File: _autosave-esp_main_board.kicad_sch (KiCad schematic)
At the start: 63 parts, among them J1 USB_C_Receptacle_USB2.0_16P, J11 Conn_01x06_Socket, J12 Conn_01x02_Socket, J13 Conn_01x02_Socket, J14 Conn_01x04_Socket, J2 Conn_01x03_Pin, J3 Conn_01x03_Pin, J4 Conn_01x03_Pin, J5 Conn_01x03_Pin, J6 Conn_01x03_Socket, J7 Conn_01x03_Socket, J8 Conn_01x03_Socket, J9 Conn_01x03_Socket, Q3 BSS138, Q4 BSS138, Q5 BSS138, Q6 BSS138, Q7 BSS138, Q8 BSS138, SW1 SW_Push, SW2 SW_Push, U1 USBLC6-2SC6, U2 AMS1117-3.3, U3 ESP32-WROOM-32, U5 CH340G, U6 TB6612FNG, Y1 Crystal_GND24

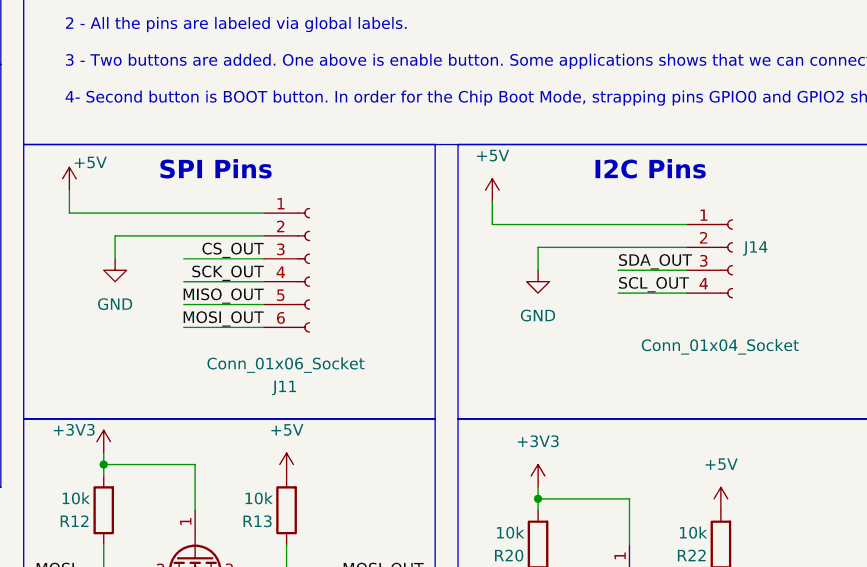
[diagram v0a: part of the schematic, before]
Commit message: feat(hw): complete schematic and PCB layout for little daisies dev board
- Add CH340G USB-to-UART bridge with 12MHz crystal oscillator and USB-C ESD protection.
- Integrate TB6612FNG dual DC motor driver with bulk decoupling capacitor.
- Add 6x BSS138 MOSFET bidirectional level-shifting circuits with 10k pull-up arrays.
- Add EN (Reset) and BOOT tactile push buttons (SW1, SW2) for firmware flashing.
- Add 4x 3-pin servo headers (J2-J5) and socket headers (J6-J9).
- Add expansion headers for IMU module (J11), motor outputs (J12, J13), and I2C/BMS (J14).
- Update PCB layout in little_daisies_dev_board.kicad_pcb with component routing.
- Add schematic wiring guide and technical component documentation.
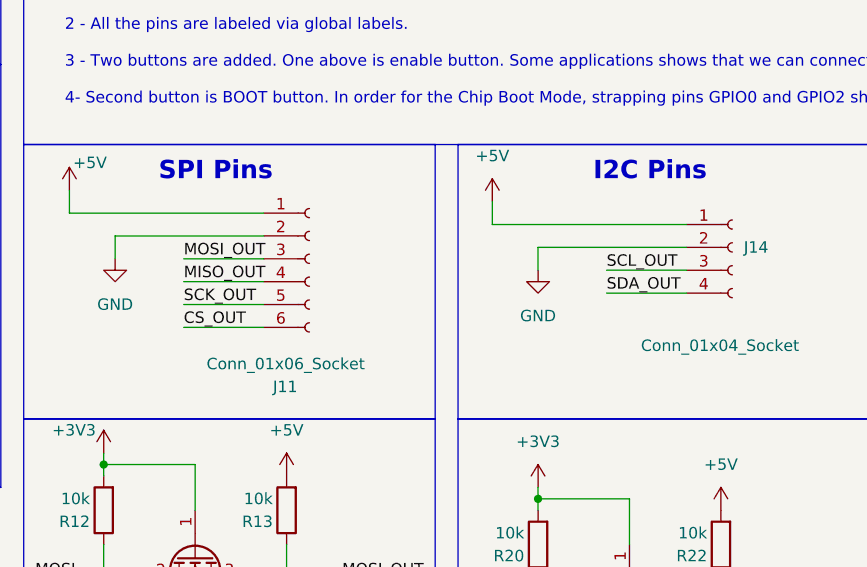
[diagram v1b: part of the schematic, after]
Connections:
- net CS_OUT: now also J11.6 (Pin_6); no longer J11.3 (Pin_3)
- net MISO_OUT: now also J11.4 (Pin_4); no longer J11.5 (Pin_5)
- net MOSI_OUT: now also J11.3 (Pin_3); no longer J11.6 (Pin_6)
- net SCK_OUT: now also J11.5 (Pin_5); no longer J11.4 (Pin_4)
- net SCL_OUT: now also J14.3 (Pin_3); no longer J14.4 (Pin_4)
- net SDA_OUT: now also J14.4 (Pin_4); no longer J14.3 (Pin_3)
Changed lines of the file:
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@@
-	(wire
-		(pts
-			(xy 146.05 163.83) (xy 137.16 163.83)
-		)
-		(stroke
-			(width 0)
-			(type default)
-		)
-	)
 	(wire
 		(pts
@@
 	(wire
 		(pts
-			(xy 185.42 162.56) (xy 193.04 162.56)
-		)
-		(stroke
-			(width 0)
-			(type default)
-		)
-	)
-	(wire
-		(pts
 			(xy 120.65 276.86) (xy 128.27 276.86)
 		)
@@
 	(wire
 		(pts
-			(xy 146.05 166.37) (xy 137.16 166.37)
-		)
-		(stroke
-			(width 0)
-			(type default)
-		)
-	)
-	(wire
-		(pts
 			(xy 252.73 95.25) (xy 256.7764 95.25)
 		)
@@
 	(wire
 		(pts
-			(xy 146.05 161.29) (xy 137.16 161.29)
+			(xy 137.16 168.91) (xy 146.05 168.91)
 		)
 		(stroke
@@
 	(wire
 		(pts
+			(xy 137.16 161.29) (xy 146.05 161.29)
+		)
+		(stroke
+			(width 0)
+			(type default)
+		)
+	)
+	(wire
+		(pts
 			(xy 181.61 228.6) (xy 176.53 228.6)
 		)
@@
 	(wire
 		(pts
-			(xy 146.05 168.91) (xy 137.16 168.91)
-		)
-		(stroke
-			(width 0)
-			(type default)
-		)
-	)
-	(wire
-		(pts
 			(xy 186.69 100.33) (xy 193.04 100.33)
 		)
@@
 	(wire
 		(pts
+			(xy 137.16 163.83) (xy 146.05 163.83)
+		)
+		(stroke
+			(width 0)
+			(type default)
+		)
+	)
+	(wire
+		(pts
 			(xy 219.71 64.77) (xy 222.25 64.77)
 		)
@@
 	(wire
 		(pts
-			(xy 185.42 165.1) (xy 193.04 165.1)
-		)
-		(stroke
-			(width 0)
-			(type default)
-		)
-	)
-	(wire
-		(pts
 			(xy 140.97 34.29) (xy 140.97 33.02)
 		)
@@
 	(wire
 		(pts
+			(xy 184.15 165.1) (xy 193.04 165.1)
+		)
+		(stroke
+			(width 0)
+			(type default)
+		)
+	)
+	(wire
+		(pts
 			(xy 186.69 82.55) (xy 193.04 82.55)
 		)
@@
 	(wire
 		(pts
+			(xy 137.16 166.37) (xy 146.05 166.37)
+		)
+		(stroke
+			(width 0)
+			(type default)
+		)
+	)
+	(wire
+		(pts
 			(xy 186.69 187.96) (xy 186.69 193.04)
 		)
@@
 		(pts
 			(xy 133.35 251.46) (xy 128.27 251.46)
+		)
+		(stroke
+			(width 0)
+			(type default)
+		)
+	)
+	(wire
+		(pts
+			(xy 184.15 162.56) (xy 193.04 162.56)
 		)
 		(stroke
@@
 	)
 	(label "CS_OUT"
-		(at 146.05 161.29 180)
-		(effects
-			(font
-				(size 1.27 1.27)
-			)
-			(justify right bottom)
+		(at 137.16 168.91 0)
+		(effects
+			(font
+				(size 1.27 1.27)
+			)
+			(justify left bottom)
 		)
 	)
@@
 	)
 	(label "MISO_OUT"
-		(at 146.05 166.37 180)
-		(effects
-			(font
-				(size 1.27 1.27)
-			)
-			(justify right bottom)
+		(at 137.16 163.83 0)
+		(effects
+			(font
+				(size 1.27 1.27)
+			)
+			(justify left bottom)
 		)
 	)
@@
 	)
 	(label "SCK_OUT"
-		(at 146.05 163.83 180)
-		(effects
-			(font
-				(size 1.27 1.27)
-			)
-			(justify right bottom)
+		(at 137.16 166.37 0)
+		(effects
+			(font
+				(size 1.27 1.27)
+			)
+			(justify left bottom)
 		)
 	)
@@
 	)
 	(label "SDA_OUT"
-		(at 185.42 162.56 0)
+		(at 184.15 165.1 0)
 		(effects
 			(font
@@
 	)
 	(label "SCL_OUT"
-		(at 185.42 165.1 0)
+		(at 184.15 162.56 0)
 		(effects
 			(font
@@
 	)
 	(label "MOSI_OUT"
-		(at 146.05 168.91 180)
-		(effects
-			(font
-				(size 1.27 1.27)
-			)
-			(justify right bottom)
-		)
-	)
+		(at 137.16 161.29 0)
+		(effects
+			(font
+				(size 1.27 1.27)
+			)
+			(justify left bottom)
+		)
+	)
